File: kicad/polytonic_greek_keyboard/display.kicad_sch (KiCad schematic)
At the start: 4 parts, among them SW1 SW_Wuerth_450301014042, SW2 RotaryEncoder_Switch_MP

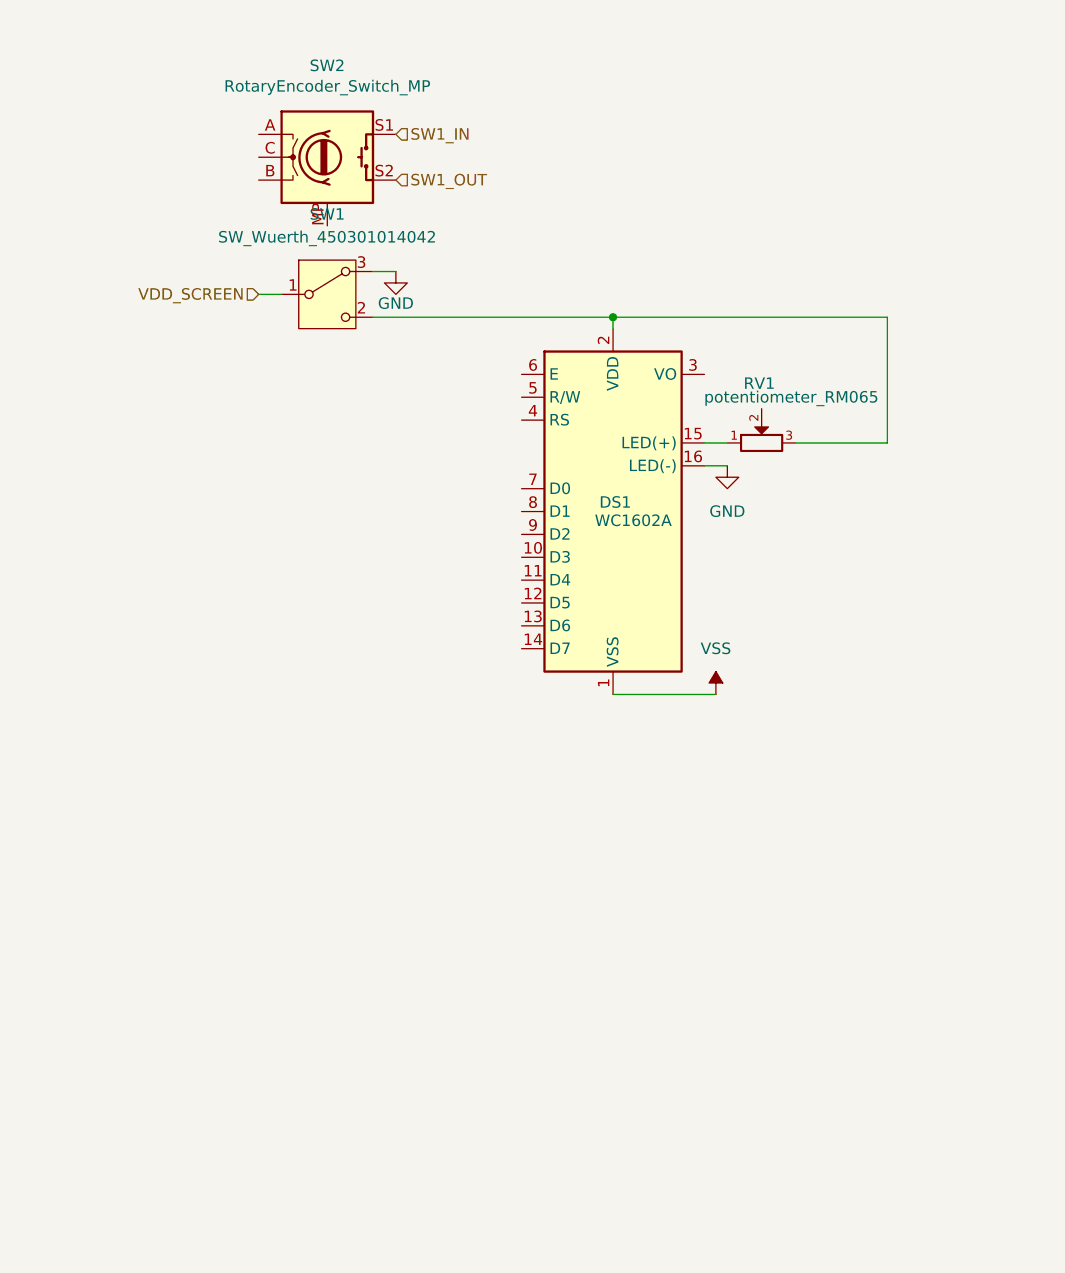
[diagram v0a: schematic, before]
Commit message: [ADD] the kicad desing of the I²C chip for the keybard
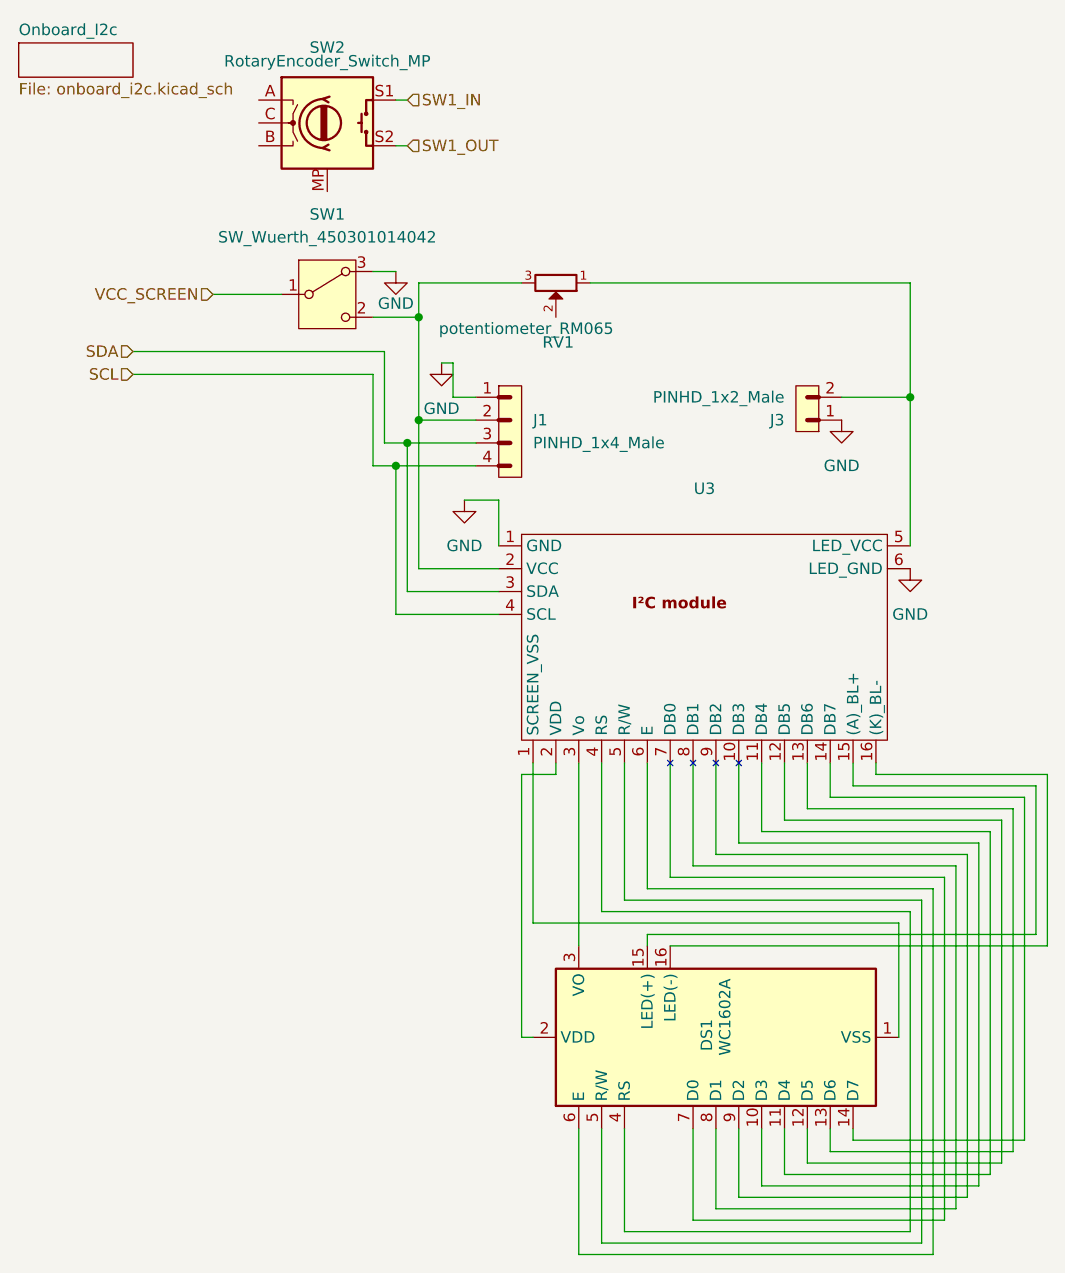
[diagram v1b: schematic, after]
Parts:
- added J1: PINHD_1x4_Male, Connector_PinHeader_2.54mm:PinHeader_1x04_P2.54mm_Vertical, symbol PCM_SL_Pin_Headers:PINHD_1x4_Male
- added J3: PINHD_1x2_Male, Connector_PinHeader_2.54mm:PinHeader_1x02_P2.54mm_Vertical, symbol PCM_SL_Pin_Headers:PINHD_1x2_Male
- added U3: ~, polytonic_greek_keyboard:I²C, symbol polytonic_greek_keyboard:I²C
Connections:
- net GND: now also J1.1, J3.1, U3.1 (SCREEN_VSS), U3.6 (LED_GND); no longer DS1.16 (LED(-))
- net at RV1.1: now also J3.2, U3.5 (LED_VCC); no longer DS1.15 (LED(+))
- net at RV1.3, SW1.2 (C): now also J1.2, U3.2 (VDD); no longer DS1.2 (VDD)
- net at DS1.10 (D3): now also U3.10 (DB3)
- net at DS1.11 (D4): now also U3.11 (DB4)
- net at DS1.12 (D5): now also U3.12 (DB5)
- net at DS1.13 (D6): now also U3.13 (DB6)
- net at DS1.14 (D7): now also U3.14 (DB7)
- net at DS1.3 (VO): now also U3.3 (Vo)
- net at DS1.4 (RS): now also U3.4 (RS)
- net at DS1.5 (R/W): now also U3.5 (LED_VCC)
- net at DS1.6 (E): now also U3.6 (LED_GND)
- net at DS1.7 (D0): now also U3.7 (DB0)
- net at DS1.8 (D1): now also U3.8 (DB1)
- net at DS1.9 (D2): now also U3.9 (DB2)
- net VDD_SCREEN renamed VCC_SCREEN
- net VSS: no longer names the net of DS1.1 (VSS)
- net VSS: now also U3.1 (SCREEN_VSS)
- new net: DS1.15 (LED(+)), U3.15 ((A)_BL+)
- new net: DS1.16 (LED(-)), U3.16 ((K)_BL-)
- new net: DS1.2 (VDD), U3.2 (VDD)
- new net SCL: J1.4, U3.4 (RS)
- new net SDA: J1.3, U3.3 (Vo)
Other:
- added sheet Onboard_I2c (onboard_i2c.kicad_sch)
- moved on the sheet: DS1, RV1, SW2

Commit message: [ADD] a more structured approach of the pcb in a way that won't overload the esp32 that is running it
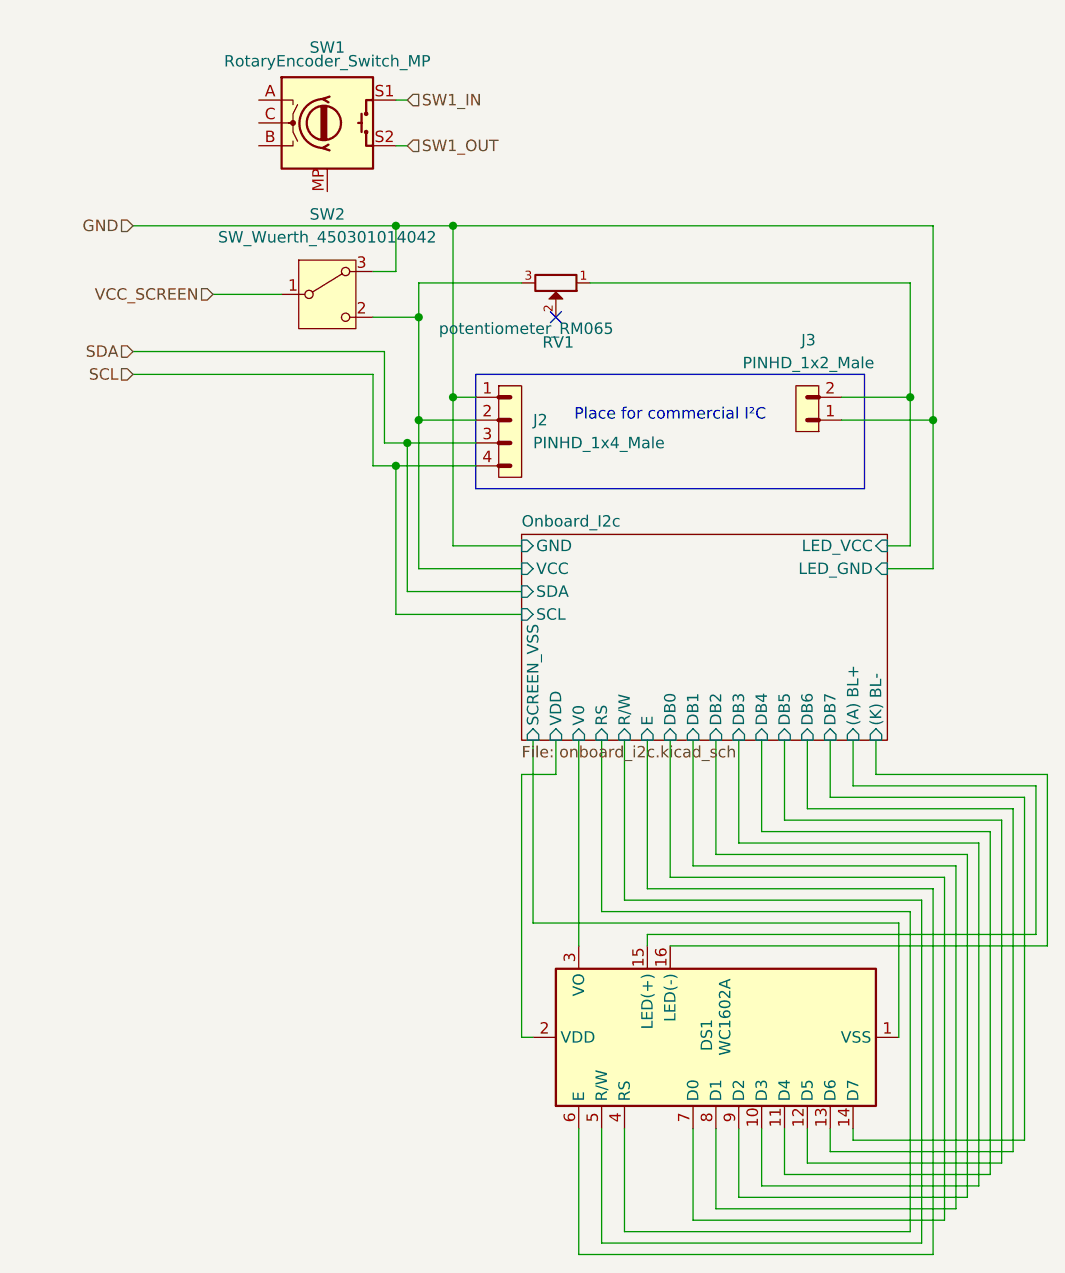
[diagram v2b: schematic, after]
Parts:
- removed U3: ~, polytonic_greek_keyboard:I²C, symbol polytonic_greek_keyboard:I²C
- SW1: renamed from SW2; footprint Rotary_Encoder:RotaryEncoder_Alps_EC11E-Switch_Vertical_H20mm_CircularMountingHoles -> Misc:RotaryEncoder_Alps_EC11E-Switch_Vertical_H20mm
- renumbered J1 to J2, SW1 to SW2
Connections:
- net Onboard_I2c/LED_VCC: now reaches J3.2, RV1.1
- net Onboard_I2c/VCC: now reaches J2.2, RV1.3, SW2.2 (C)
- net Onboard_I2c/SCREEN_VSS: now reaches DS1.1 (VSS)
- net Onboard_I2c/DB3: now reaches DS1.10 (D3)
- net Onboard_I2c/DB4: now reaches DS1.11 (D4)
- net Onboard_I2c/DB5: now reaches DS1.12 (D5)
- net Onboard_I2c/DB6: now reaches DS1.13 (D6)
- net Onboard_I2c/DB7: now reaches DS1.14 (D7)
- net Onboard_I2c/(A) BL+: now reaches DS1.15 (LED(+))
- net Onboard_I2c/(K) BL-: now reaches DS1.16 (LED(-))
- net Onboard_I2c/VDD: now reaches DS1.2 (VDD)
- net Onboard_I2c/V0: now reaches DS1.3 (VO)
- net Onboard_I2c/RS: now reaches DS1.4 (RS)
- net Onboard_I2c/R/W: now reaches DS1.5 (R/W)
- net Onboard_I2c/E: now reaches DS1.6 (E)
- net Onboard_I2c/DB0: now reaches DS1.7 (D0)
- net Onboard_I2c/DB1: now reaches DS1.8 (D1)
- net Onboard_I2c/DB2: now reaches DS1.9 (D2)
- no-connect marks 0 -> 1
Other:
- sheet Onboard_I2c ports: added (A) BL+, (K) BL-, DB0, DB1, DB2, DB3, DB4, DB5, DB6, DB7, E, GND, LED_GND, LED_VCC, RS, R/W, SCL, SCREEN_VSS, SDA, V0, VCC, VDD; removed none
- note added: "Place for commercial I²C"

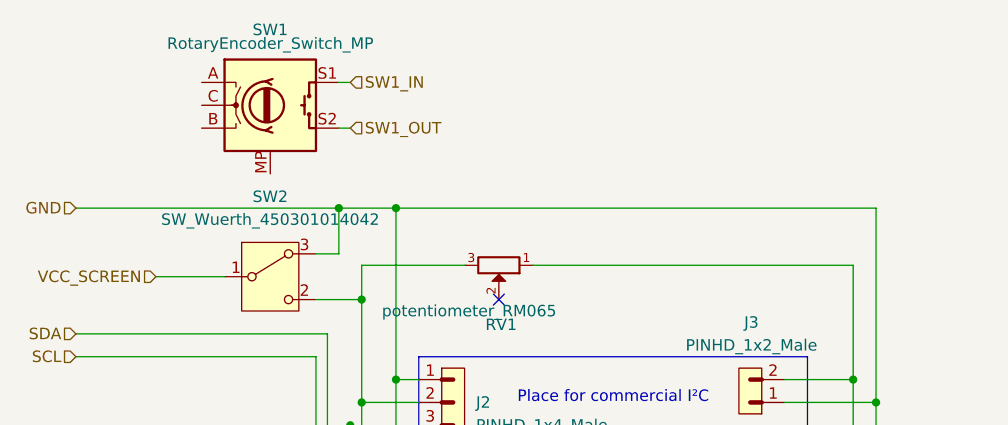
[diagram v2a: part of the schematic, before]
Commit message: [UPDATE] the board desing, [FIX] connection issues
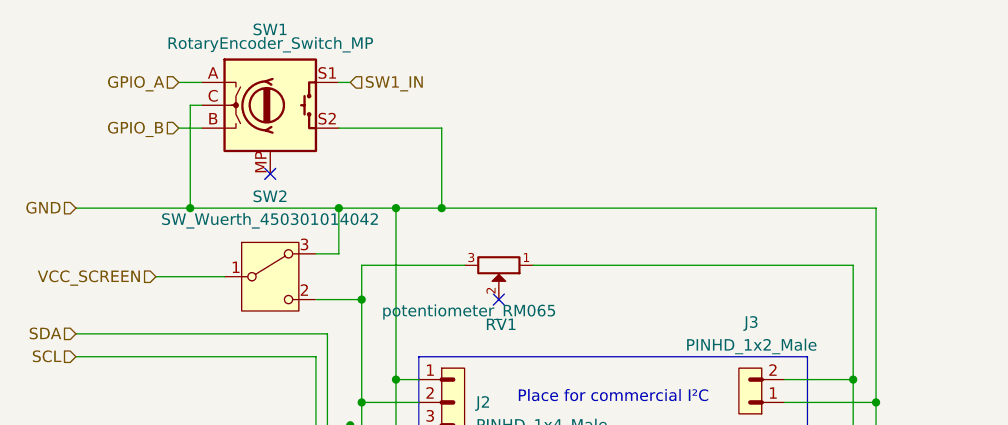
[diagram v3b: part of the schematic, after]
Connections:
- net SW1_OUT is gone; now on net GND: SW1.S2
- net GND: now also SW1.C
- net GPIO_A: now reaches SW1.A
- net GPIO_B: now reaches SW1.B
- no-connect marks 1 -> 2
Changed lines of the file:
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@@
 	)
 	(junction
+		(at 38.1 33.02)
+		(diameter 0)
+		(color 0 0 0 0)
+	)
+	(junction
 		(at 55.88 57.15)
 		(diameter 0)
@@
 	)
 	(junction
+		(at 66.04 33.02)
+		(diameter 0)
+		(color 0 0 0 0)
+	)
+	(junction
 		(at 60.96 52.07)
 		(diameter 0)
@@
 	)
 	(no_connect
+		(at 46.99 29.21)
+	)
+	(no_connect
 		(at 72.39 43.18)
 	)
@@
 	(wire
 		(pts
+			(xy 38.1 33.02) (xy 54.61 33.02)
+		)
+		(stroke
+			(width 0)
+			(type default)
+		)
+	)
+	(wire
+		(pts
 			(xy 118.11 140.97) (xy 118.11 102.87)
 		)
@@
 	(wire
 		(pts
+			(xy 36.83 24.13) (xy 39.37 24.13)
+		)
+		(stroke
+			(width 0)
+			(type default)
+		)
+	)
+	(wire
+		(pts
 			(xy 92.71 140.97) (xy 118.11 140.97)
 		)
@@
 	(wire
 		(pts
-			(xy 114.3 33.02) (xy 60.96 33.02)
+			(xy 114.3 33.02) (xy 66.04 33.02)
 		)
 		(stroke
@@
 	(wire
 		(pts
+			(xy 39.37 21.59) (xy 38.1 21.59)
+		)
+		(stroke
+			(width 0)
+			(type default)
+		)
+	)
+	(wire
+		(pts
 			(xy 123.19 97.79) (xy 100.33 97.79)
 		)
@@
 	(wire
 		(pts
-			(xy 25.4 33.02) (xy 54.61 33.02)
+			(xy 25.4 33.02) (xy 38.1 33.02)
 		)
 		(stroke
@@
 	(wire
 		(pts
+			(xy 36.83 19.05) (xy 39.37 19.05)
+		)
+		(stroke
+			(width 0)
+			(type default)
+		)
+	)
+	(wire
+		(pts
 			(xy 60.96 33.02) (xy 60.96 52.07)
 		)
@@
 	(wire
 		(pts
-			(xy 54.61 24.13) (xy 55.88 24.13)
+			(xy 54.61 24.13) (xy 66.04 24.13)
+		)
+		(stroke
+			(width 0)
+			(type default)
+		)
+	)
+	(wire
+		(pts
+			(xy 66.04 33.02) (xy 60.96 33.02)
 		)
 		(stroke
@@
 	(wire
 		(pts
+			(xy 38.1 21.59) (xy 38.1 33.02)
+		)
+		(stroke
+			(width 0)
+			(type default)
+		)
+	)
+	(wire
+		(pts
 			(xy 69.85 110.49) (xy 110.49 110.49)
 		)
@@
 	(wire
 		(pts
+			(xy 66.04 24.13) (xy 66.04 33.02)
+		)
+		(stroke
+			(width 0)
+			(type default)
+		)
+	)
+	(wire
+		(pts
 			(xy 123.19 135.89) (xy 123.19 97.79)
 		)
@@
 		)
 	)
-	(hierarchical_label "SW1_OUT"
+	(hierarchical_label "GPIO_A"
 		(shape input)
-		(at 55.88 24.13 0)
+		(at 36.83 19.05 180)
 		(effects
 			(font
 				(size 1.27 1.27)
 			)
-			(justify left)
+			(justify right)
 		)
 	)
@@
 		)
 	)
+	(hierarchical_label "GPIO_B"
+		(shape input)
+		(at 36.83 24.13 180)
+		(effects
+			(font
+				(size 1.27 1.27)
+			)
+			(justify right)
+		)
+	)

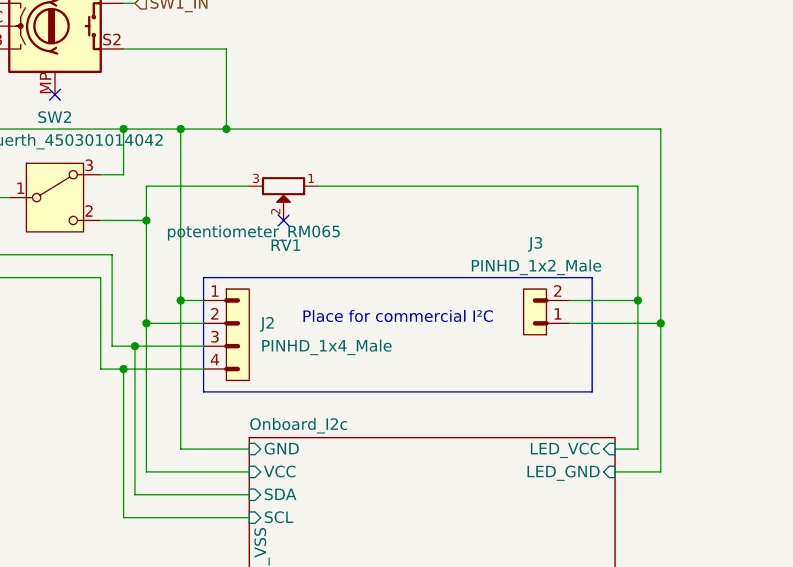
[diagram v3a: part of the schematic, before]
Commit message: [UPDATE] the desing to fit on two separate pcbs
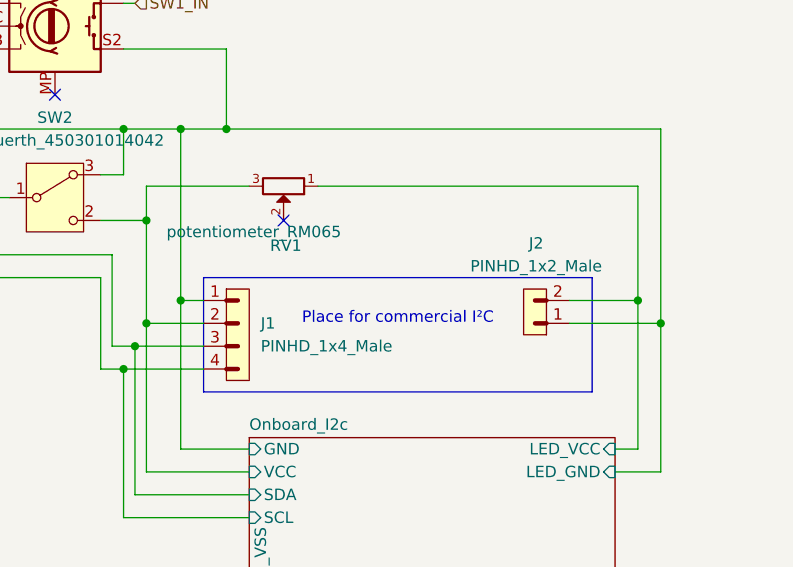
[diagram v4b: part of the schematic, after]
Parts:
- renumbered J2 to J1, J3 to J2
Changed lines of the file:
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@@
 		(dnp no)
 		(fields_autoplaced yes)
-		(property "Reference" "J3"
+		(property "Reference" "J2"
 			(at 100.455 45.72 0)
 			(effects
@@
 		)
 		(instances
-			(project ""
-				(path "/cbe25a1b-6c02-43c2-9ff9-ba274c7cf6a2/b9347469-4bb2-4648-b4dc-d6f3187000d0"
-					(reference "J3")
+			(project "polytonic_greek_keyboard"
+				(path "/cbe25a1b-6c02-43c2-9ff9-ba274c7cf6a2/8498b325-11fd-4b20-a704-75ec3d8987ef/ec54e47a-8e8b-4416-b579-fc6e7c329b94"
+					(reference "J2")
 					(unit 1)
 				)
@@
 		)
 		(instances
-			(project ""
-				(path "/cbe25a1b-6c02-43c2-9ff9-ba274c7cf6a2/b9347469-4bb2-4648-b4dc-d6f3187000d0"
+			(project "polytonic_greek_keyboard"
+				(path "/cbe25a1b-6c02-43c2-9ff9-ba274c7cf6a2/8498b325-11fd-4b20-a704-75ec3d8987ef/ec54e47a-8e8b-4416-b579-fc6e7c329b94"
 					(reference "SW1")
 					(unit 1)
@@
 		)
 		(instances
-			(project ""
-				(path "/29d1f4c4-2c66-4ff7-ad76-620f460314f7/4b4f3352-d2ed-45db-938e-9f7a16254cad"
-					(reference "RV1")
-					(unit 1)
-				)
-			)
-			(project ""
-				(path "/cbe25a1b-6c02-43c2-9ff9-ba274c7cf6a2/b9347469-4bb2-4648-b4dc-d6f3187000d0"
+			(project "polytonic_greek_keyboard"
+				(path "/cbe25a1b-6c02-43c2-9ff9-ba274c7cf6a2/8498b325-11fd-4b20-a704-75ec3d8987ef/ec54e47a-8e8b-4416-b579-fc6e7c329b94"
 					(reference "RV1")
 					(unit 1)
@@
 		)
 		(instances
-			(project ""
-				(path "/cbe25a1b-6c02-43c2-9ff9-ba274c7cf6a2/b9347469-4bb2-4648-b4dc-d6f3187000d0"
+			(project "polytonic_greek_keyboard"
+				(path "/cbe25a1b-6c02-43c2-9ff9-ba274c7cf6a2/8498b325-11fd-4b20-a704-75ec3d8987ef/ec54e47a-8e8b-4416-b579-fc6e7c329b94"
 					(reference "SW2")
 					(unit 1)
@@
 		(dnp no)
 		(fields_autoplaced yes)
-		(property "Reference" "J2"
+		(property "Reference" "J1"
 			(at 69.85 54.6099 0)
 			(effects
@@
 		)
 		(instances
-			(project ""
-				(path "/cbe25a1b-6c02-43c2-9ff9-ba274c7cf6a2/b9347469-4bb2-4648-b4dc-d6f3187000d0"
-					(reference "J2")
+			(project "polytonic_greek_keyboard"
+				(path "/cbe25a1b-6c02-43c2-9ff9-ba274c7cf6a2/8498b325-11fd-4b20-a704-75ec3d8987ef/ec54e47a-8e8b-4416-b579-fc6e7c329b94"
+					(reference "J1")
 					(unit 1)
 				)
@@
 		)
 		(instances
-			(project ""
-				(path "/cbe25a1b-6c02-43c2-9ff9-ba274c7cf6a2/b9347469-4bb2-4648-b4dc-d6f3187000d0"
+			(project "polytonic_greek_keyboard"
+				(path "/cbe25a1b-6c02-43c2-9ff9-ba274c7cf6a2/8498b325-11fd-4b20-a704-75ec3d8987ef/ec54e47a-8e8b-4416-b579-fc6e7c329b94"
 					(reference "DS1")
 					(unit 1)
@@
 		(instances
 			(project "polytonic_greek_keyboard"
-				(path "/cbe25a1b-6c02-43c2-9ff9-ba274c7cf6a2/b9347469-4bb2-4648-b4dc-d6f3187000d0"
-					(page "7")
-				)
-			)
+				(path "/cbe25a1b-6c02-43c2-9ff9-ba274c7cf6a2/8498b325-11fd-4b20-a704-75ec3d8987ef/ec54e47a-8e8b-4416-b579-fc6e7c329b94"
+					(page "4")
+				)
+			)

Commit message: [UPDATE] the final merged version of the schematic before splitting into two separate kicad projects
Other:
- company: (none) -> Henry's Software House
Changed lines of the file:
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@@
 	(generator_version "9.0")
 	(paper "A4")
+	(title_block
+		(rev "1 - do not edit connector pin layout.")
+		(company "Henry's Software House")
+	)
 	(rectangle
 		(start 63.5 49.53)
